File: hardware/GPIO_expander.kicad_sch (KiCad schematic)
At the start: 2 parts

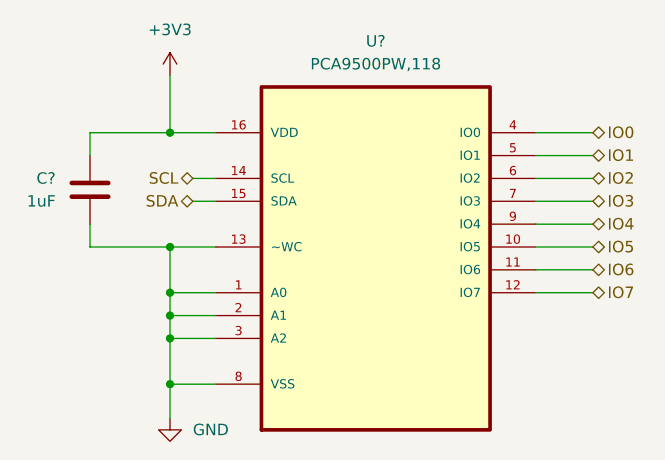
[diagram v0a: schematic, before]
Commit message: Replace PCA9500 I/O expander with TCA9534
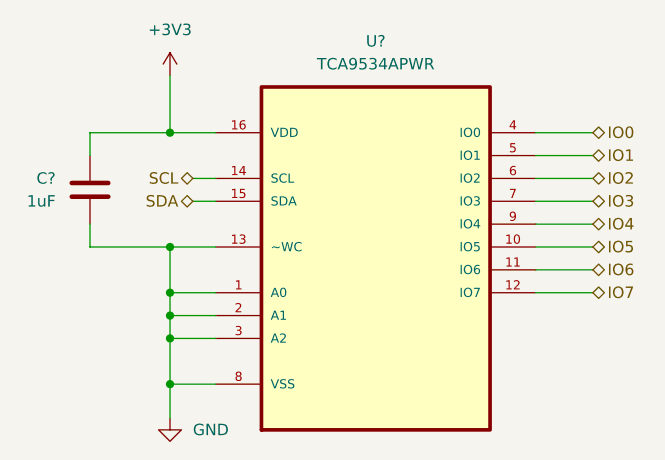
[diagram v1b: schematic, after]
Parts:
- U?: value PCA9500PW,118 -> TCA9534APWR; Availability In Stock -> (none); Check_prices https://www.snapeda.com/parts/PCA9500PW,118/NXP+USA+Inc./vi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 -> (none); MF NXP USA -> (none); MP PCA9500PW,118 -> (none); MPN PCA9500PW,118 -> (none); OC_FARNELL - -> (none); OC_NEWARK 70R6438 -> (none); PACKAGE TSSOP -> (none); Package TSSOP-16 NXP Semiconductors -> (none); Price None -> (none); Purchase-URL https://www.snapeda.com/api/url_track_click_mouser/?unipart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 -> (none); SUPPLIER NXP -> (none); SnapEDA_Link https://www.snapeda.com/parts/PCA9500PW,118/NXP+USA+Inc./vi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 -> (none)
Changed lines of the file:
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@@
       (effects (font (size 1.27 1.27)))
     )
-    (property "Value" "PCA9500PW,118" (at 139.7 81.28 0)
+    (property "Value" "TCA9534APWR" (at 139.7 81.28 0)
       (effects (font (size 1.27 1.27)))
     )
@@
       (effects (font (size 1.27 1.27)) (justify bottom) hide)
     )
-    (property "Datasheet" "" (at 139.7 99.06 0)
+    (property "Datasheet" "https://www.ti.com/general/docs/suppproductinfo.tsp?distId=10&gotoUrl=https%3A%2F%2Fwww.ti.com%2Flit%2Fgpn%2Ftca9534a" (at 139.7 99.06 0)
       (effects (font (size 1.27 1.27)) hide)
     )
-    (property "MF" "NXP USA" (at 139.7 99.06 0)
+    (property "Description" "I/O Expander 8 I2C 400 kHz 16-TSSOP" (at 139.7 99.06 0)
       (effects (font (size 1.27 1.27)) (justify bottom) hide)
     )
-    (property "Description" "\nI/O Expander 8 I²C, SMBus 400 kHz 16-TSSOP\n" (at 139.7 99.06 0)
-      (effects (font (size 1.27 1.27)) (justify bottom) hide)
-    )
-    (property "PACKAGE" "TSSOP" (at 139.7 99.06 0)
-      (effects (font (size 1.27 1.27)) (justify bottom) hide)
-    )
-    (property "MPN" "PCA9500PW,118" (at 139.7 99.06 0)
-      (effects (font (size 1.27 1.27)) (justify bottom) hide)
-    )
-    (property "Price" "None" (at 139.7 99.06 0)
-      (effects (font (size 1.27 1.27)) (justify bottom) hide)
-    )
-    (property "Package" "TSSOP-16 NXP Semiconductors" (at 139.7 99.06 0)
-      (effects (font (size 1.27 1.27)) (justify bottom) hide)
-    )
-    (property "OC_FARNELL" "-" (at 139.7 99.06 0)
-      (effects (font (size 1.27 1.27)) (justify bottom) hide)
-    )
-    (property "SnapEDA_Link" "https://www.snapeda.com/parts/PCA9500PW,118/NXP+USA+Inc./view-part/?ref=snap" (at 139.7 99.06 0)
-      (effects (font (size 1.27 1.27)) (justify bottom) hide)
-    )
-    (property "MP" "PCA9500PW,118" (at 139.7 99.06 0)
-      (effects (font (size 1.27 1.27)) (justify bottom) hide)
-    )
-    (property "Purchase-URL" "https://www.snapeda.com/api/url_track_click_mouser/?unipart_id=32896&manufacturer=NXP USA&part_name=PCA9500PW,118&search_term=pca9500" (at 139.7 99.06 0)
-      (effects (font (size 1.27 1.27)) (justify bottom) hide)
-    )
-    (property "SUPPLIER" "NXP" (at 139.7 99.06 0)
-      (effects (font (size 1.27 1.27)) (justify bottom) hide)
-    )
-    (property "OC_NEWARK" "70R6438" (at 139.7 99.06 0)
-      (effects (font (size 1.27 1.27)) (justify bottom) hide)
-    )
-    (property "Availability" "In Stock" (at 139.7 99.06 0)
-      (effects (font (size 1.27 1.27)) (justify bottom) hide)
-    )
-    (property "Check_prices" "https://www.snapeda.com/parts/PCA9500PW,118/NXP+USA+Inc./view-part/?ref=eda" (at 139.7 99.06 0)
-      (effects (font (size 1.27 1.27)) (justify bottom) hide)
-    )
